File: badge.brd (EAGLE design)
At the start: 27.9 x 45.7 mm, 3 parts

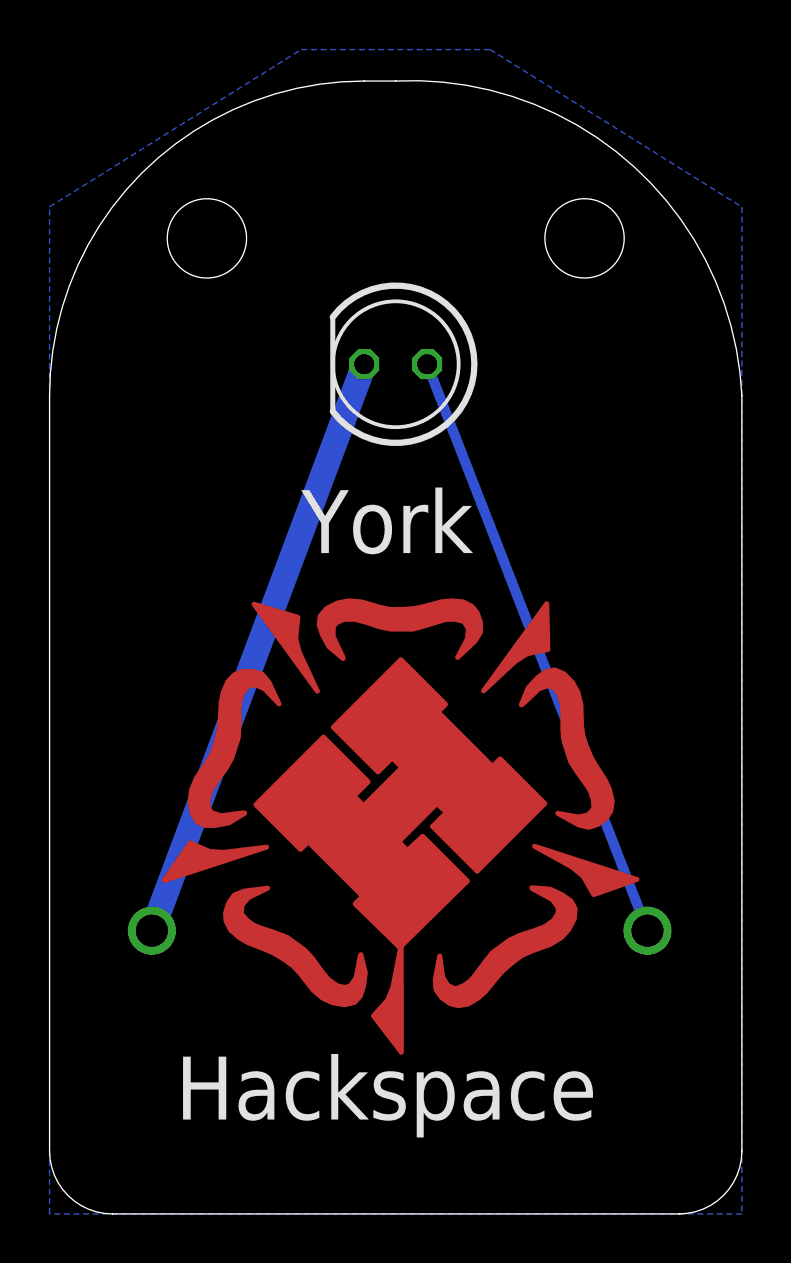
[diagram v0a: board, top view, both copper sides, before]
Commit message: Fixed polarity
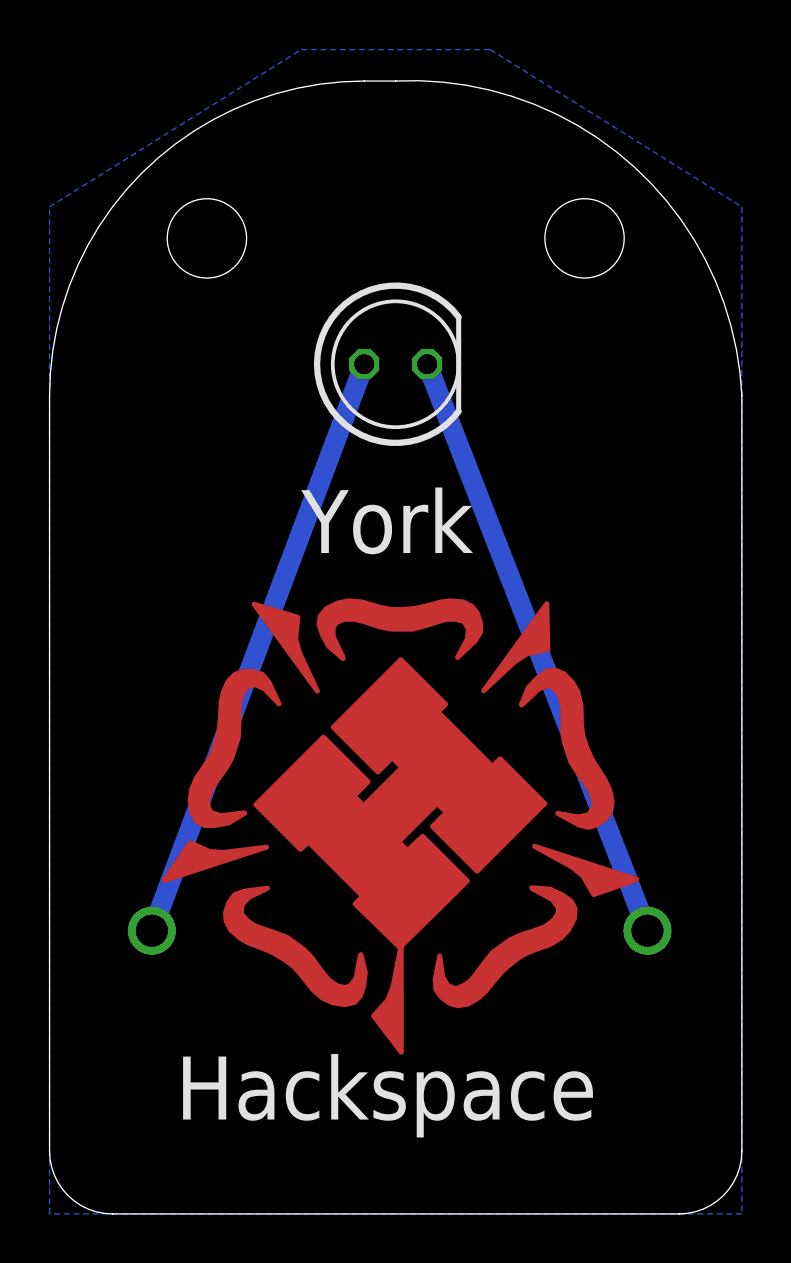
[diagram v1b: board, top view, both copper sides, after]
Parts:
- turned LED1 to 0 degrees
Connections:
- net GND: now also LED1.K; no longer LED1.A
- net N$2: now also LED1.A; no longer LED1.K
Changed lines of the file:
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@@
 <attribute name="VALUE" x="31.115" y="10.795" size="0.4064" layer="28" rot="MR0"/>
 </element>
-<element name="LED1" library="led" package="LED5MM" value="" x="13.97" y="34.29" smashed="yes" rot="R180">
-<attribute name="VALUE" x="10.7696" y="36.0934" size="1.27" layer="27" ratio="10" rot="R180"/>
+<element name="LED1" library="led" package="LED5MM" value="" x="13.97" y="34.29" smashed="yes">
+<attribute name="VALUE" x="17.1704" y="32.4866" size="1.27" layer="27" ratio="10"/>
 </element>
 <element name="U$1" library="YHSLogo" package="YHSLOGO_FANCY" value="YHSLOGOFANCY" x="13.97" y="16.51"/>
@@
 <signal name="GND">
 <contactref element="BAT1" pad="2"/>
-<contactref element="LED1" pad="A"/>
-<wire x1="15.24" y1="34.29" x2="24.13" y2="11.43" width="0.4064" layer="16"/>
 <polygon width="0.4064" layer="16" isolate="0.8128">
 <vertex x="27.94" y="0"/>
@@
 <vertex x="27.94" y="40.64"/>
 </polygon>
+<contactref element="LED1" pad="K"/>
+<wire x1="15.24" y1="34.29" x2="24.13" y2="11.43" width="0.8128" layer="16"/>
 </signal>
 <signal name="N$2">
-<contactref element="LED1" pad="K"/>
 <contactref element="BAT1" pad="1"/>
-<wire x1="12.7" y1="34.29" x2="4.13" y2="11.43" width="1.016" layer="16"/>
+<contactref element="LED1" pad="A"/>
+<wire x1="4.13" y1="11.43" x2="12.7" y2="34.29" width="0.8128" layer="16"/>
 </signal>
 </signals>
